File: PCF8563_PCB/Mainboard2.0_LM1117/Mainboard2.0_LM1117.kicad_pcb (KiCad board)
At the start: 2 copper layers, 40 parts, among them J1 CONN_01X03, J2 USB_B, J4 SD_Card, J5 CONN_01X03, J6 CONN_01X02, J7 CONN_01X02, Q1 BC847, Q2 BC847, SW1 SW_DIP_x01, U1 LM1117-3.3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

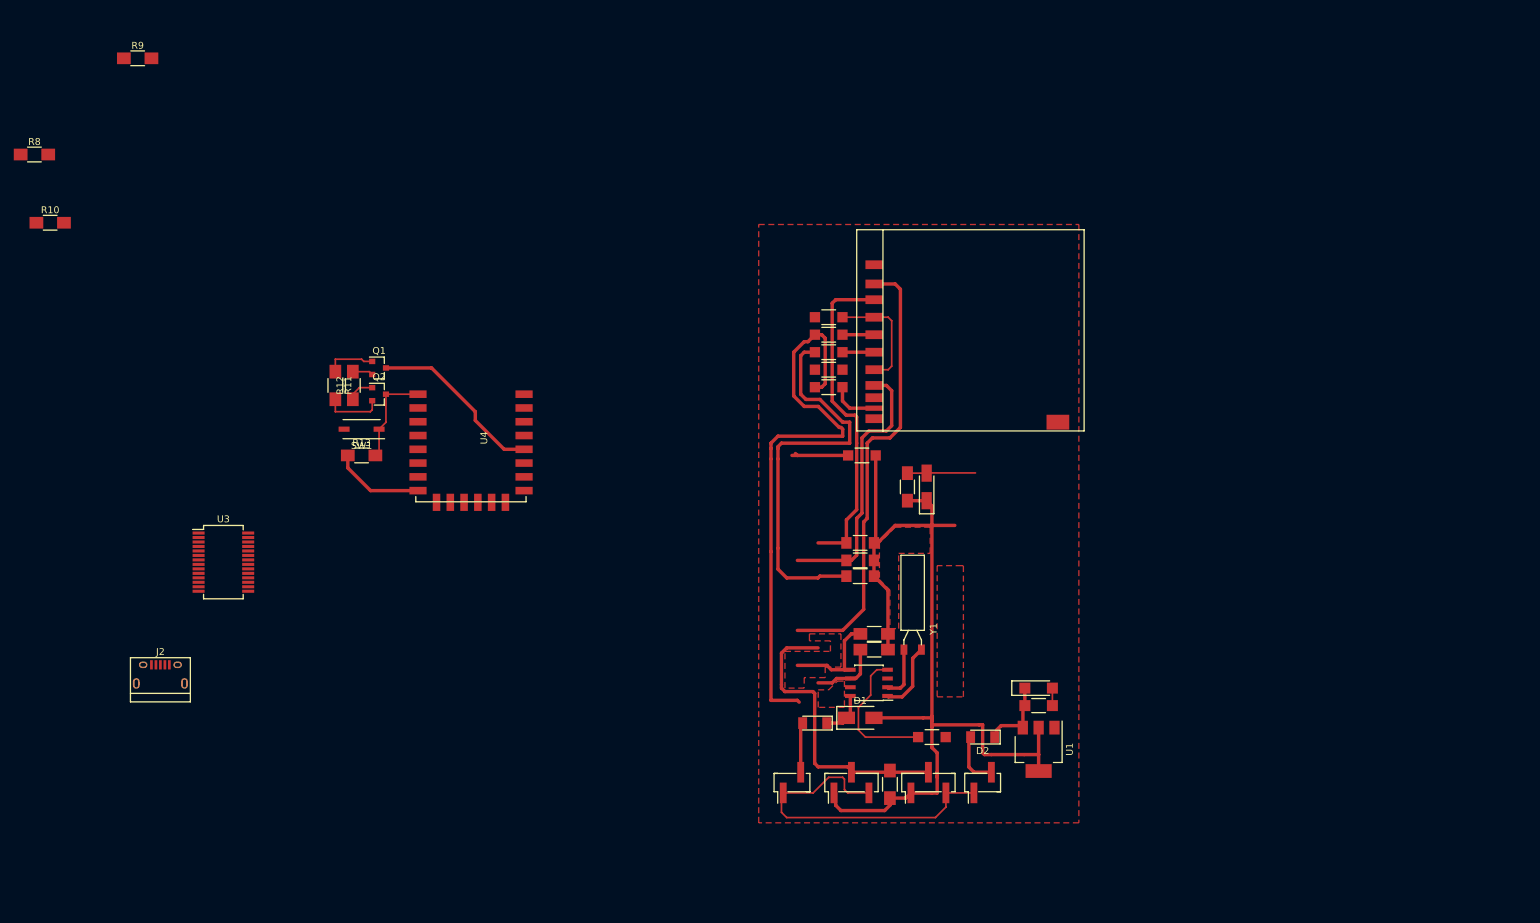
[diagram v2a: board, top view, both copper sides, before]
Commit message: SMD board complete
Full SMD board is complete - needs to be tested though. Looks kinda awful, large SD card slot is taking lots of space.
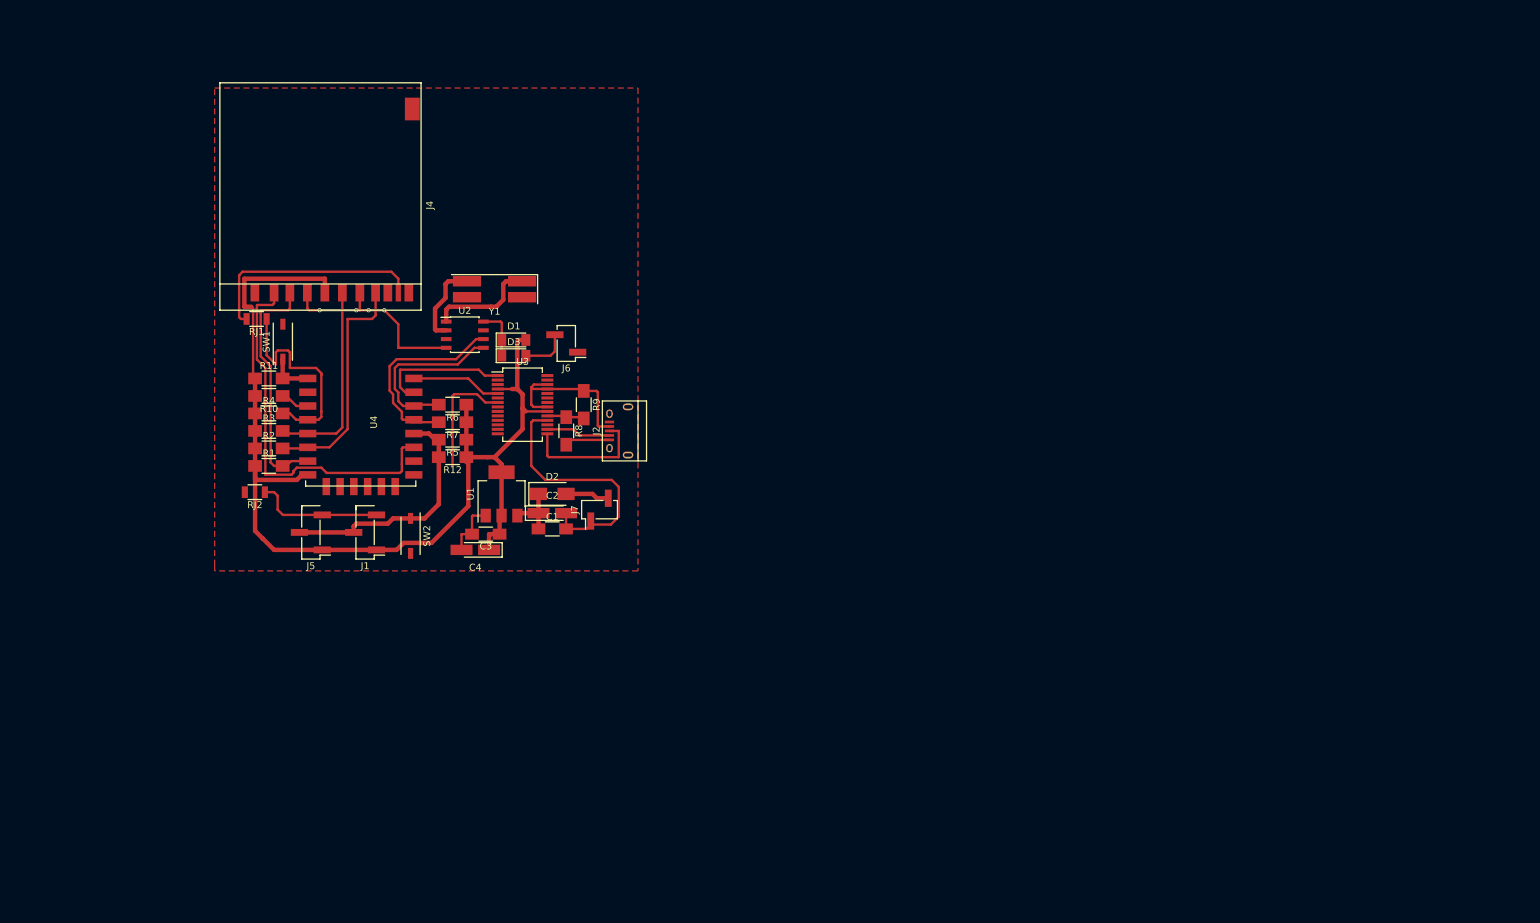
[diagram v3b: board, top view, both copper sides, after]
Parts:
- removed Q1, Q2: BC847, TO_SOT_Packages_SMD:SOT-23
- removed R13: 1k, Resistors_SMD:R_1206_HandSoldering
- removed RJ3, RJ4, RJ5, RJ6: 0, Resistors_SMD:R_1206_HandSoldering
- added SW2: FLASH, Buttons_Switches_SMD:SW_DIP_x1_W5.08mm_Slide_Copal_CHS-A, F.Cu at (79.5, 98.0)
- D1: footprint Diodes_SMD:D_SMA -> Diodes_SMD:D_MiniMELF
- D2: footprint Diodes_SMD:D_MiniMELF -> Diodes_SMD:D_SMA
- J4: footprint Moje:SDCARD-STANDARD -> dodatki:SDCARD-STANDARD
- R11, R12: value 10k -> 1k
- RJ1, RJ2: footprint Resistors_SMD:R_1206_HandSoldering -> Resistors_SMD:R_1206
- SW1: value SW_DIP_x01 -> RESET
- Y1: footprint Crystals:Crystal_AT310_d3.0mm_l10.0mm_Horizontal -> Crystals:Crystal_SMD_SeikoEpson_MC406-4pin_9.6x4.1mm
- moved J4 109.8 mm to (60.7, 41.1), turned to 270 degrees
- moved J1 89.5 mm to (72.9, 97.5), turned to 180 degrees
- moved R3 88.4 mm to (58.9, 82.8), turned to 0 degrees
- moved RJ2 88.3 mm to (56.9, 91.7), turned to 180 degrees
- moved R2 87.4 mm to (58.9, 85.3), turned to 0 degrees
- moved R8 87.0 mm to (102.1, 82.8), turned to 270 degrees
- moved R1 86.6 mm to (58.9, 87.9), turned to 0 degrees
- moved J5 86.5 mm to (65.0, 97.5), turned to 180 degrees
- moved U1 86.3 mm to (92.7, 91.9), turned to 90 degrees
- moved RJ1 83.2 mm to (57.1, 66.5), turned to 180 degrees
- moved R4 82.1 mm to (58.9, 80.3), turned to 0 degrees
- moved R9 82.0 mm to (104.6, 79.0), turned to 270 degrees
- moved Y1 81.1 mm to (91.7, 62.2)
- moved R5 80.8 mm to (85.6, 84.1), turned to 180 degrees
- moved U2 77.4 mm to (87.4, 68.8), turned to 0 degrees
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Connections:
- J4 pad 5: SCK -> GPIO14
- R11 pad 1: Net-(Q1-Pad1) -> 3V3
- R11 pad 2: RTS -> RESET
- R12 pad 1: Net-(Q2-Pad1) -> 3V3
- R12 pad 2: DTR -> 1wire
- R4 pad 2: GPIO16 -> SD_D
- RJ1 pad 1: GPIO14 -> SD_D
- RJ1 pad 2: SCK -> Net-(J4-Pad10)
- RJ2 pad 1: 3V3 -> GND
- RJ2 pad 2: 3V3 -> GND
- U3 pad 2: DTR -> (no net)
- U3 pad 3: RTS -> (no net)
- U4 pad 4: GPIO16 -> SD_D
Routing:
- net GPIO16: track 81.6 -> 0.00 mm
- net 1wire: track 68.7 -> 36.5 mm
- net SD_D: track 0.00 -> 31.4 mm
- net GND: track 104.6 -> 135.8 mm, vias 0 -> 4
- net GPIO14: track 58.7 -> 28.9 mm
- net Net-(J4-Pad10): track 3.56 -> 33.2 mm
- net GPIO4: track 10.2 -> 29.2 mm
- net Net-(J2-Pad3): track 0.00 -> 18.8 mm
- net Rx: track 0.00 -> 18.7 mm
- net Tx: track 0.00 -> 13.8 mm
- net GPIO13: track 48.1 -> 35.9 mm
- net CS: track 65.2 -> 54.5 mm
- net GPIO5: track 14.9 -> 25.3 mm
- net Net-(J2-Pad2): track 0.00 -> 9.39 mm
- net RTS: track 8.59 -> 0.00 mm
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- removed copper zone on F.Cu, net (none)
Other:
- net class Default: trace_width 0.25 -> 0.35
- net class Grubsze: trace_width 0.5 -> 0.65
- rule pad_to_mask_clearance: 0.2 -> 0
- board text removed: "C2"
- board text removed: "C3"
